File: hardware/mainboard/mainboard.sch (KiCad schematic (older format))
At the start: 19 parts

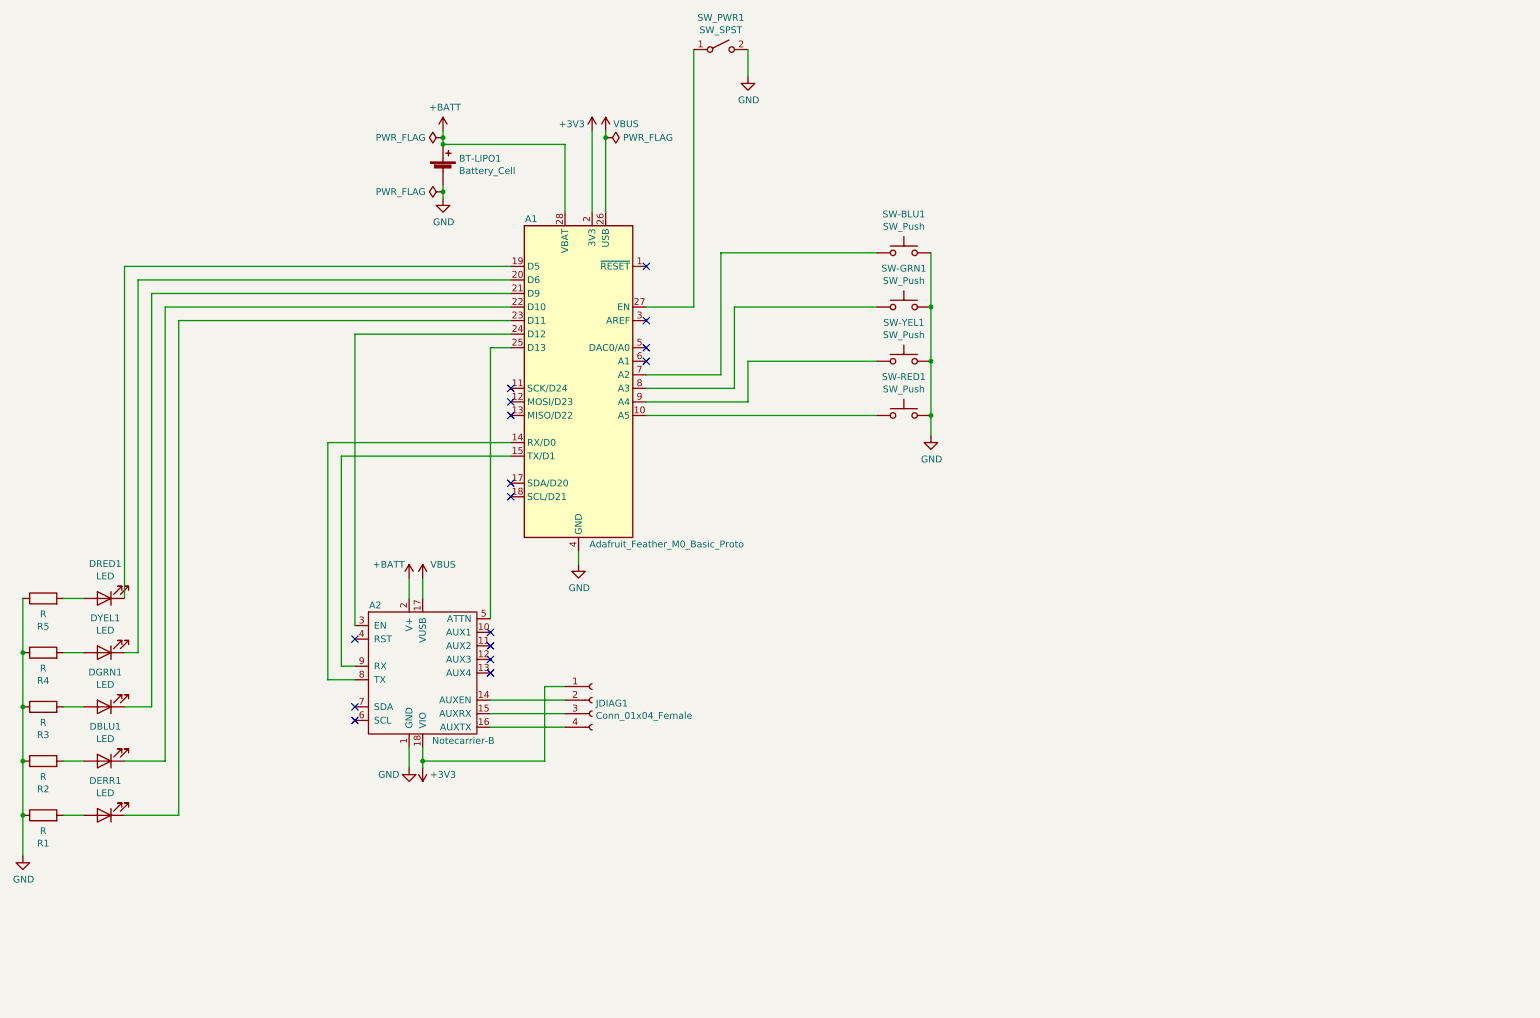
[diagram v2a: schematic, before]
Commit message: Record Ethan's Comments
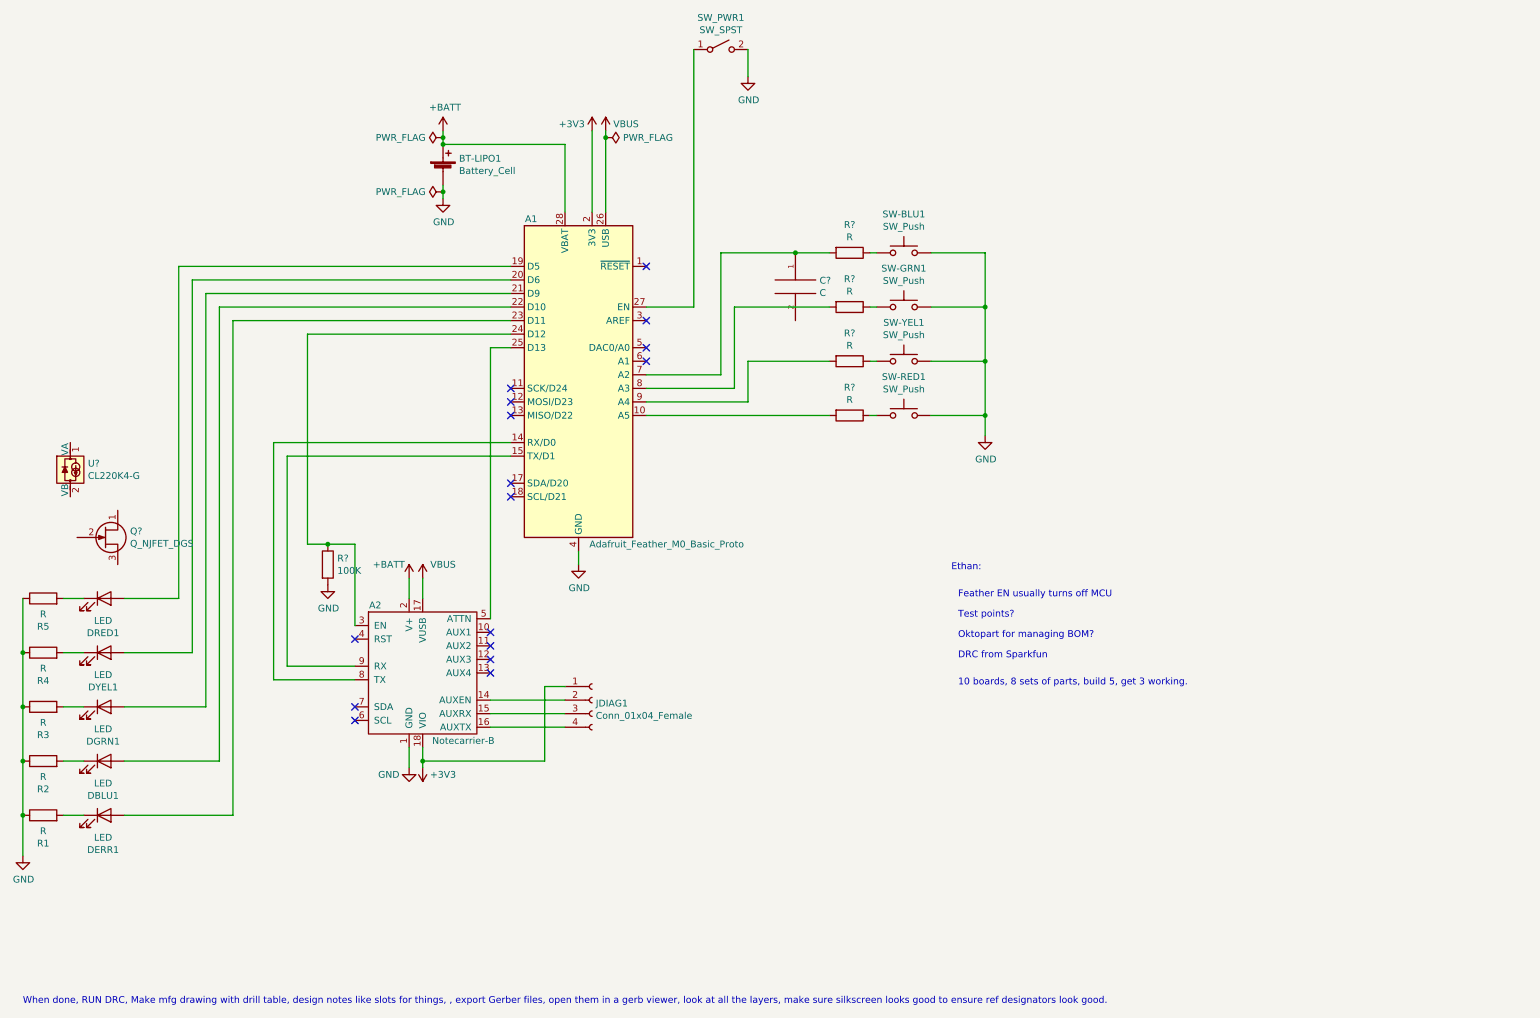
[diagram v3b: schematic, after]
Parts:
- added C?: C, symbol pspice:C
- added Q?: Q_NJFET_DGS, symbol Device:Q_NJFET_DGS
- added R?: 100K, symbol Device:R
- added R? (x4): R, symbol Device:R
- added U?: CL220K4-G, Package_TO_SOT_SMD:TO-252-2, symbol Driver_LED:CL220K4-G
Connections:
- net GND: now also R?.2
- net at DRED1.1 (K): now also R5.2; no longer A1.19 (D5)
- net at DRED1.2 (A): now also A1.19 (D5); no longer R5.2
- net at DYEL1.1 (K): now also R4.2; no longer A1.20 (D6)
- net at DYEL1.2 (A): now also A1.20 (D6); no longer R4.2
- net at DBLU1.1 (K): now also R2.2; no longer A1.22 (D10)
- net at DBLU1.2 (A): now also A1.22 (D10); no longer R2.2
- net at DGRN1.1 (K): now also R3.2; no longer A1.21 (D9)
- net at DGRN1.2 (A): now also A1.21 (D9); no longer R3.2
- net at DERR1.1 (K): now also R1.2; no longer A1.23 (D11)
- net at DERR1.2 (A): now also A1.23 (D11); no longer R1.2
- net at SW-RED1.1: now also R?.1; no longer A1.10 (A5)
- net at SW-YEL1.1: now also R?.1; no longer A1.9 (A4)
- net at SW-GRN1.1: now also R?.1; no longer A1.8 (A3)
- net at SW-BLU1.1: now also R?.1; no longer A1.7 (A2)
- net at A1.24 (D12), A2.3 (EN): now also R?.1
- new net: A1.10 (A5), R?.2
- new net: A1.7 (A2), C?.1, R?.2
- new net: A1.8 (A3), R?.2
- new net: A1.9 (A4), R?.2
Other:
- note added: "10 boards, 8 sets of parts, build 5, get 3 working."
- note added: "DRC from Sparkfun"
- note added: "Ethan:"
- note added: "Feather EN usually turns off MCU"
- note added: "Oktopart for managing BOM?"
- note added: "Test points?"
- note added: "When done, RUN DRC, Make mfg drawing with drill table, design notes like slots for things, , export Gerber files, open them in a gerb viewer, look at all the layers, make sure silkscreen looks good to ensure ref designators look good."
- moved on the sheet: DBLU1, DERR1, DGRN1, DRED1, DYEL1
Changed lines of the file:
@@
 Comment1 ""
 Comment2 ""
-Comment3 ""
+Comment3 "Ethan's Comments"
 Comment4 "Dreadflint"
 $EndDescr
@@
 F 3 "~" H 1650 5300 50  0001 C CNN
 	1    1650 5300
-	-1   0    0    1
+	1    0    0    -1
 $EndComp
 $Comp
@@
 F 3 "~" H 1650 5700 50  0001 C CNN
 	1    1650 5700
-	-1   0    0    1
+	1    0    0    -1
 $EndComp
 $Comp
@@
 F 3 "~" H 1650 6500 50  0001 C CNN
 	1    1650 6500
-	-1   0    0    1
+	1    0    0    -1
 $EndComp
 $Comp
@@
 F 3 "~" H 1650 6100 50  0001 C CNN
 	1    1650 6100
-	-1   0    0    1
+	1    0    0    -1
 $EndComp
 $Comp
@@
 F 3 "~" H 1650 6900 50  0001 C CNN
 	1    1650 6900
-	-1   0    0    1
+	1    0    0    -1
 $EndComp
 $Comp
@@
 $EndComp
 Wire Wire Line
-	4650 2850 1800 2850
-Wire Wire Line
-	1800 2850 1800 5300
-Wire Wire Line
-	4650 2950 1900 2950
+	4650 2850 2200 2850
+Wire Wire Line
+	4650 2950 2300 2950
 Wire Wire Line
 	1500 6900 1350 6900
@@
 	6300 3750 6300 3150
 Wire Wire Line
-	6300 3150 7350 3150
-Wire Wire Line
-	7350 2750 6200 2750
+	6300 3150 7000 3150
+Wire Wire Line
+	7350 2750 7300 2750
 Wire Wire Line
 	6200 3650 5650 3650
@@
 L power:GND #PWR0103
 U 1 1 61BF33A5
-P 7750 4100
-F 0 "#PWR0103" H 7750 3850 50  0001 C CNN
-F 1 "GND" H 7755 3927 50  0000 C CNN
-F 2 "" H 7750 4100 50  0001 C CNN
-F 3 "" H 7750 4100 50  0001 C CNN
-	1    7750 4100
+P 8150 4100
+F 0 "#PWR0103" H 8150 3850 50  0001 C CNN
+F 1 "GND" H 8155 3927 50  0000 C CNN
+F 2 "" H 8150 4100 50  0001 C CNN
+F 3 "" H 8150 4100 50  0001 C CNN
+	1    8150 4100
 	1    0    0    -1
 $EndComp
@@
 Wire Wire Line
 	5350 2450 5350 1900
-Wire Wire Line
-	3500 5500 3500 3350
 $Comp
 L power:+3V3 #PWR02
@@
 	6400 3850 6400 3550
 Wire Wire Line
-	6400 3550 7350 3550
+	6400 3550 7000 3550
 $Comp
 L power:+BATT #PWR0106
@@
 	3900 6400 3900 6550
 Wire Wire Line
-	4650 4150 3300 4150
-Wire Wire Line
-	3300 5900 3500 5900
-Wire Wire Line
-	3300 4150 3300 5900
-Wire Wire Line
-	3500 5800 3400 5800
-Wire Wire Line
-	3400 5800 3400 4250
-Wire Wire Line
-	3400 4250 4650 4250
-Wire Wire Line
-	3500 3350 4650 3350
+	4650 4150 2900 4150
+Wire Wire Line
+	2900 5900 3500 5900
+Wire Wire Line
+	2900 4150 2900 5900
+Wire Wire Line
+	3500 5800 3000 5800
+Wire Wire Line
+	3000 5800 3000 4250
+Wire Wire Line
+	3000 4250 4650 4250
 Wire Wire Line
 	4500 3450 4500 5450
@@
 	1050 6900 1050 7200
 Wire Wire Line
-	7750 2750 7750 3150
-Connection ~ 7750 3150
-Wire Wire Line
-	7750 3150 7750 3550
-Connection ~ 7750 3550
-Wire Wire Line
-	7750 3550 7750 3950
-Connection ~ 7750 3950
-Wire Wire Line
-	7750 3950 7750 4100
-Wire Wire Line
-	2000 3050 2000 6100
-Wire Wire Line
-	2000 6100 1800 6100
-Wire Wire Line
-	2000 3050 4650 3050
-Wire Wire Line
-	2100 6500 2100 3150
-Wire Wire Line
-	2100 3150 4650 3150
-Wire Wire Line
-	1800 6500 2100 6500
-Wire Wire Line
-	4650 3250 2200 3250
-Wire Wire Line
-	2200 3250 2200 6900
-Wire Wire Line
-	2200 6900 1800 6900
-Wire Wire Line
-	1900 2950 1900 5700
-Wire Wire Line
-	1900 5700 1800 5700
+	2400 3050 2400 6100
+Wire Wire Line
+	2400 6100 1800 6100
+Wire Wire Line
+	2400 3050 4650 3050
+Wire Wire Line
+	2500 6500 2500 3150
+Wire Wire Line
+	2500 3150 4650 3150
+Wire Wire Line
+	1800 6500 2500 6500
+Wire Wire Line
+	4650 3250 2600 3250
+Wire Wire Line
+	2600 3250 2600 6900
+Wire Wire Line
+	2600 6900 1800 6900
+Wire Wire Line
+	2300 2950 2300 5700
+Wire Wire Line
+	2300 5700 1800 5700
 Wire Wire Line
 	6200 2750 6200 3650
 Wire Wire Line
-	5650 3950 7350 3950
+	5650 3950 7000 3950
 Wire Wire Line
 	4150 1950 4150 1900
@@
 Wire Wire Line
 	6000 1250 6000 3150
+Wire Wire Line
+	1800 5300 2200 5300
+Wire Wire Line
+	2200 5300 2200 2850
+Text Notes 7900 5100 0    50   ~ 0
+Ethan:
+Text Notes 7950 5300 0    50   ~ 0
+Feather EN usually turns off MCU
+$Comp
+L Device:R R?
+U 1 1 61C1679A
+P 3300 5050
+F 0 "R?" H 3370 5096 50  0000 L CNN
+F 1 "100K" H 3370 5005 50  0000 L CNN
+F 2 "" V 3230 5050 50  0001 C CNN
+F 3 "~" H 3300 5050 50  0001 C CNN
+	1    3300 5050
+	1    0    0    -1
+$EndComp
+$Comp
+L power:GND #PWR?
+U 1 1 61C1688E
+P 3300 5200
+F 0 "#PWR?" H 3300 4950 50  0001 C CNN
+F 1 "GND" H 3305 5027 50  0000 C CNN
+F 2 "" H 3300 5200 50  0001 C CNN
+F 3 "" H 3300 5200 50  0001 C CNN
+	1    3300 5200
+	1    0    0    -1
+$EndComp
+$Comp
+L Device:R R?
+U 1 1 61C168E5
+P 7150 3950
+F 0 "R?" V 6943 3950 50  0000 C CNN
+F 1 "R" V 7034 3950 50  0000 C CNN
+F 2 "" V 7080 3950 50  0001 C CNN
+F 3 "~" H 7150 3950 50  0001 C CNN
+	1    7150 3950
+	0    1    1    0
+$EndComp
+Wire Wire Line
+	7300 3950 7350 3950
+$Comp
+L Device:R R?
+U 1 1 61C16A13
+P 7150 3550
+F 0 "R?" V 6943 3550 50  0000 C CNN
+F 1 "R" V 7034 3550 50  0000 C CNN
+F 2 "" V 7080 3550 50  0001 C CNN
+F 3 "~" H 7150 3550 50  0001 C CNN
+	1    7150 3550
+	0    1    1    0
+$EndComp
+Wire Wire Line
+	7300 3550 7350 3550
+$Comp
+L Device:R R?
+U 1 1 61C16A63
+P 7150 3150
+F 0 "R?" V 6943 3150 50  0000 C CNN
+F 1 "R" V 7034 3150 50  0000 C CNN
+F 2 "" V 7080 3150 50  0001 C CNN
+F 3 "~" H 7150 3150 50  0001 C CNN
+	1    7150 3150
+	0    1    1    0
+$EndComp
+Wire Wire Line
+	7300 3150 7350 3150
+$Comp
+L Device:R R?
+U 1 1 61C16AB1
+P 7150 2750
+F 0 "R?" V 6943 2750 50  0000 C CNN
+F 1 "R" V 7034 2750 50  0000 C CNN
+F 2 "" V 7080 2750 50  0001 C CNN
+F 3 "~" H 7150 2750 50  0001 C CNN
+	1    7150 2750
+	0    1    1    0
+$EndComp
+Wire Wire Line
+	7000 2750 6750 2750
+Wire Wire Line
+	7750 2750 8150 2750
+Wire Wire Line
+	8150 2750 8150 3150
+Wire Wire Line
+	7750 3150 8150 3150
+Connection ~ 8150 3150
+Wire Wire Line
+	8150 3150 8150 3550
+Wire Wire Line
+	7750 3550 8150 3550
+Connection ~ 8150 3550
+Wire Wire Line
+	8150 3550 8150 3950
+Wire Wire Line
+	7750 3950 8150 3950
+Connection ~ 8150 3950
+Wire Wire Line
+	8150 3950 8150 4100
+$Comp
+L pspice:C C?
+U 1 1 61C25C96
+P 6750 3000
+F 0 "C?" H 6928 3046 50  0000 L CNN
+F 1 "C" H 6928 2955 50  0000 L CNN
+F 2 "" H 6750 3000 50  0001 C CNN
+F 3 "~" H 6750 3000 50  0001 C CNN
+	1    6750 3000
+	1    0    0    -1
+$EndComp
+Connection ~ 6750 2750
+Wire Wire Line
+	6750 2750 6200 2750
+$Comp
+L Device:Q_NJFET_DGS Q?
+U 1 1 61C3DE63
+P 1650 4850
+F 0 "Q?" H 1841 4896 50  0000 L CNN
+F 1 "Q_NJFET_DGS" H 1841 4805 50  0000 L CNN
+F 2 "" H 1850 4950 50  0001 C CNN
+F 3 "~" H 1650 4850 50  0001 C CNN
+	1    1650 4850
+	1    0    0    -1
+$EndComp
+$Comp
+L Driver_LED:CL220K4-G U?
+U 1 1 61C3E50C
+P 1400 4350
+F 0 "U?" H 1530 4396 50  0000 L CNN
+F 1 "CL220K4-G" H 1530 4305 50  0000 L CNN
+F 2 "Package_TO_SOT_SMD:TO-252-2" H 1550 4300 50  0001 L CNN
+F 3 "http://ww1.microchip.com/downloads/en/DeviceDoc/20005413A.pdf" H 1410 4350 50  0001 C CNN
+	1    1400 4350
+	1    0    0    -1
+$EndComp
+Text Notes 7950 5450 0    50   ~ 0
+Test points?
+Text Notes 7950 5600 0    50   ~ 0
+Oktopart for managing BOM?
+Text Notes 7950 5750 0    50   ~ 0
+DRC from Sparkfun
+Text Notes 1050 8300 0    50   ~ 0
+When done, RUN DRC, Make mfg drawing with drill table, design notes like slots for things, , export Gerber files, open them in a gerb viewer, look at all the layers, make sure silkscreen looks good to ensure ref designators look good.
+Text Notes 7950 5950 0    50   ~ 0
+10 boards, 8 sets of parts, build 5, get 3 working.
+Wire Wire Line
+	3500 5500 3500 4900
+Wire Wire Line
+	3500 4900 3300 4900
+Wire Wire Line
+	3150 4900 3150 3350
+Connection ~ 3300 4900
+Wire Wire Line
+	3300 4900 3150 4900
+Wire Wire Line
+	3150 3350 4650 3350
 $EndSCHEMATC
